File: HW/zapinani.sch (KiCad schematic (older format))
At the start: 2 parts

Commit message: add some packages
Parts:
- Q?: footprint (none) -> Package_TO_SOT_SMD:SOT-23
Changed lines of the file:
@@
 F 0 "Q?" V 5442 2750 50  0000 C CNN
 F 1 "Q_PMOS_DGS" V 5351 2750 50  0000 C CNN
-F 2 "" H 5300 2850 50  0001 C CNN
+F 2 "Package_TO_SOT_SMD:SOT-23" H 5300 2850 50  0001 C CNN
 F 3 "~" H 5100 2750 50  0001 C CNN
 	1    5100 2750

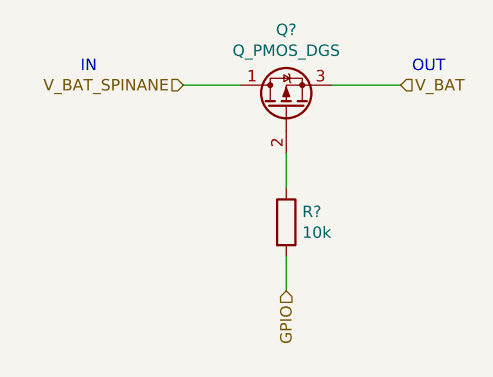
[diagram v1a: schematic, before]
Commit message: add reverse polarity protection
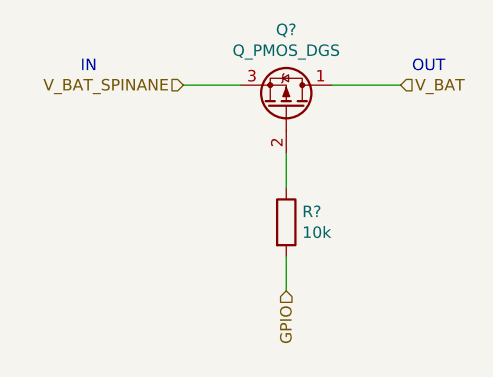
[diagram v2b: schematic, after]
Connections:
- net V_BAT: now also Q?.1 (D); no longer Q?.3 (S)
- net V_BAT_SPINANE: now also Q?.3 (S); no longer Q?.1 (D)
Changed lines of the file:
@@
 $Descr A4 11693 8268
 encoding utf-8
-Sheet 22 42
+Sheet 17 43
 Title ""
 Date ""
@@
 F 3 "~" H 5100 2750 50  0001 C CNN
 	1    5100 2750
-	0    -1   -1   0
+	0    1    -1   0
 $EndComp
 $Comp
@@
 Wire Wire Line
 	5100 3400 5100 3550
+Text HLabel 5100 3550 3    50   Input ~ 0
+GPIO
+Text HLabel 4650 2650 0    50   Input ~ 0
+V_BAT_SPINANE
 Text Notes 4200 2600 0    50   ~ 0
 IN\n
 Text Notes 5650 2600 0    50   ~ 0
 OUT\n
-Text HLabel 4650 2650 0    50   Input ~ 0
-V_BAT_SPINANE
-Text HLabel 5100 3550 3    50   Input ~ 0
-GPIO
 Text HLabel 5600 2650 2    50   Input ~ 0
 V_BAT

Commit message: add some codes for JLCPCB, change package and schematic of CP2102
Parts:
- R?: LCSC (none) -> C25744
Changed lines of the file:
@@
 F 2 "Resistor_SMD:R_0402_1005Metric" V 5030 3250 50  0001 C CNN
 F 3 "~" H 5100 3250 50  0001 C CNN
+F 4 "C25744" H 5100 3250 50  0001 C CNN "LCSC"
 	1    5100 3250
 	1    0    0    -1

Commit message: add some codes for JLCPCB
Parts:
- Q?: LCSC (none) -> C15127
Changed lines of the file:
@@
 F 2 "Package_TO_SOT_SMD:SOT-23" H 5300 2850 50  0001 C CNN
 F 3 "~" H 5100 2750 50  0001 C CNN
+F 4 "C15127" H 5100 2750 50  0001 C CNN "LCSC"
 	1    5100 2750
 	0    1    -1   0

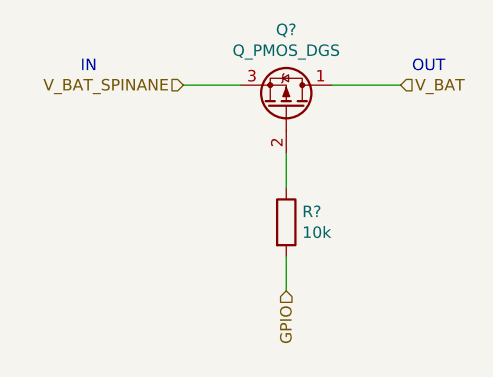
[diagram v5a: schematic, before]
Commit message: numbering components, place components on board
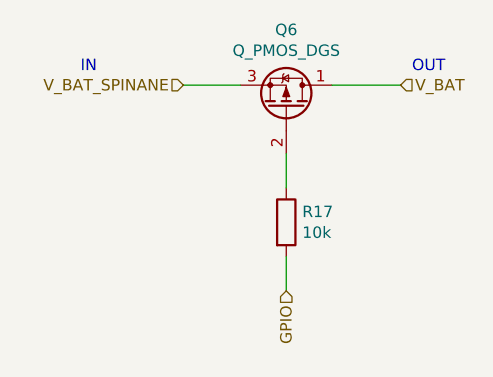
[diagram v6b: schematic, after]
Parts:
- gave numbers to parts that had none: 2
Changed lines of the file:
@@
 AR Path="/5F746478" Ref="Q?"  Part="1"
 AR Path="/5F7BA54B/5F746478" Ref="Q?"  Part="1"
-AR Path="/5F7BA54B/5F7BCB45/5F746478" Ref="Q?"  Part="1"
-AR Path="/5F7BA54B/5F7BCBA6/5F746478" Ref="Q?"  Part="1"
-AR Path="/5F7BA54B/5F7BCC0A/5F746478" Ref="Q?"  Part="1"
-AR Path="/5F7BA54B/5F7BCC69/5F746478" Ref="Q?"  Part="1"
-F 0 "Q?" V 5442 2750 50  0000 C CNN
+AR Path="/5F7BA54B/5F7BCB45/5F746478" Ref="Q3"  Part="1"
+AR Path="/5F7BA54B/5F7BCBA6/5F746478" Ref="Q4"  Part="1"
+AR Path="/5F7BA54B/5F7BCC0A/5F746478" Ref="Q5"  Part="1"
+AR Path="/5F7BA54B/5F7BCC69/5F746478" Ref="Q6"  Part="1"
+F 0 "Q6" V 5442 2750 50  0000 C CNN
 F 1 "Q_PMOS_DGS" V 5351 2750 50  0000 C CNN
 F 2 "Package_TO_SOT_SMD:SOT-23" H 5300 2850 50  0001 C CNN
@@
 AR Path="/5F74647E" Ref="R?"  Part="1"
 AR Path="/5F7BA54B/5F74647E" Ref="R?"  Part="1"
-AR Path="/5F7BA54B/5F7BCB45/5F74647E" Ref="R?"  Part="1"
-AR Path="/5F7BA54B/5F7BCBA6/5F74647E" Ref="R?"  Part="1"
-AR Path="/5F7BA54B/5F7BCC0A/5F74647E" Ref="R?"  Part="1"
-AR Path="/5F7BA54B/5F7BCC69/5F74647E" Ref="R?"  Part="1"
-F 0 "R?" H 5170 3296 50  0000 L CNN
+AR Path="/5F7BA54B/5F7BCB45/5F74647E" Ref="R14"  Part="1"
+AR Path="/5F7BA54B/5F7BCBA6/5F74647E" Ref="R15"  Part="1"
+AR Path="/5F7BA54B/5F7BCC0A/5F74647E" Ref="R16"  Part="1"
+AR Path="/5F7BA54B/5F7BCC69/5F74647E" Ref="R17"  Part="1"
+F 0 "R17" H 5170 3296 50  0000 L CNN
 F 1 "10k" H 5170 3205 50  0000 L CNN
 F 2 "Resistor_SMD:R_0402_1005Metric" V 5030 3250 50  0001 C CNN

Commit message: repair package of TP4056
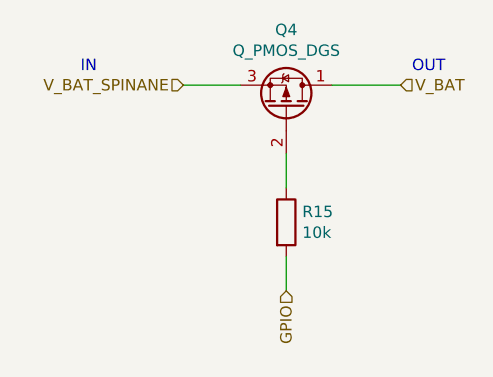
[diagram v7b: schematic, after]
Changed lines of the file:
@@
 $Descr A4 11693 8268
 encoding utf-8
-Sheet 17 44
+Sheet 18 44
 Title ""
 Date ""
@@
 AR Path="/5F7BA54B/5F7BCC0A/5F746478" Ref="Q5"  Part="1"
 AR Path="/5F7BA54B/5F7BCC69/5F746478" Ref="Q6"  Part="1"
-F 0 "Q6" V 5442 2750 50  0000 C CNN
+F 0 "Q4" V 5442 2750 50  0000 C CNN
 F 1 "Q_PMOS_DGS" V 5351 2750 50  0000 C CNN
 F 2 "Package_TO_SOT_SMD:SOT-23" H 5300 2850 50  0001 C CNN
@@
 AR Path="/5F7BA54B/5F7BCC0A/5F74647E" Ref="R16"  Part="1"
 AR Path="/5F7BA54B/5F7BCC69/5F74647E" Ref="R17"  Part="1"
-F 0 "R17" H 5170 3296 50  0000 L CNN
+F 0 "R15" H 5170 3296 50  0000 L CNN
 F 1 "10k" H 5170 3205 50  0000 L CNN
 F 2 "Resistor_SMD:R_0402_1005Metric" V 5030 3250 50  0001 C CNN
